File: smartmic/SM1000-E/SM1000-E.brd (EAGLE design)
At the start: 65 x 100 mm, 201 parts, among them CN1 HDR100-3, CN10 ST-3509, CN11 HDR100-3, CN12 HRS-A3C-16DA, CN13 CONN-BOOM-XH-2A, CN2 JS-MU3-002, CN3 DS-0518, CN4 RJ-45, CN5 ST-3509, CN6 ST-3509, CN7 ST-3509, CN8 ST-3509, CN9 ST-3509, J1 JMP-2PIN, J3 JMP-2PIN, J4 JMP-2PIN, P1 TPAD50, P10 TPAD50, P11 TPAD50, P12 TPAD50, P13 TPAD50, P14 TPAD50, P16 TPAD50, P18 TPAD50, P19 TPAD50, P2 TPAD50, P20 TPAD50, P3 TPAD50, P4 TPAD50, P5 TPAD50, P6 TPAD50, P7 TPAD50, P8 TPAD50, P9 TPAD50, SW1 SW-SPDT-8US8WR2C2M7RES, SW2 TS-026, SW3 DPDT, SW4 TS-026, SW5 TS-02B, SW6 SW-LC2259, SW7 SW-LC2259, T1 SM-LP-5001, T2 SM-LP-5001, U1 STM32F405VGT6, U2 LD3985M33R, U3 STMPS2141, U4 EMIF02-USB03F2, U5 TPS54329E, U6 LMV341, U7 LMV341, U8 LM386M-1, U9 LMV341

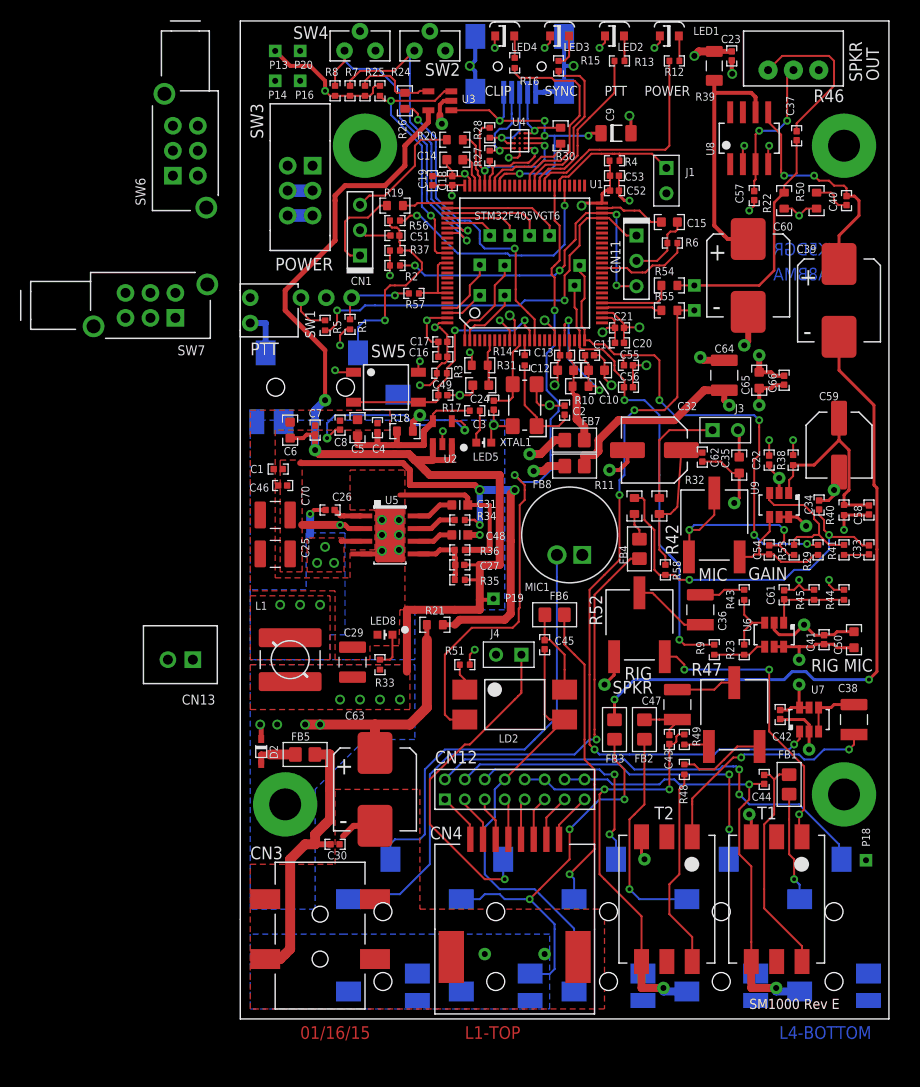
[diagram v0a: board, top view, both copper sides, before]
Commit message: IMPLEMENT CHANGES PER SM1000-E-CHANGE-LOG.TXT RGB
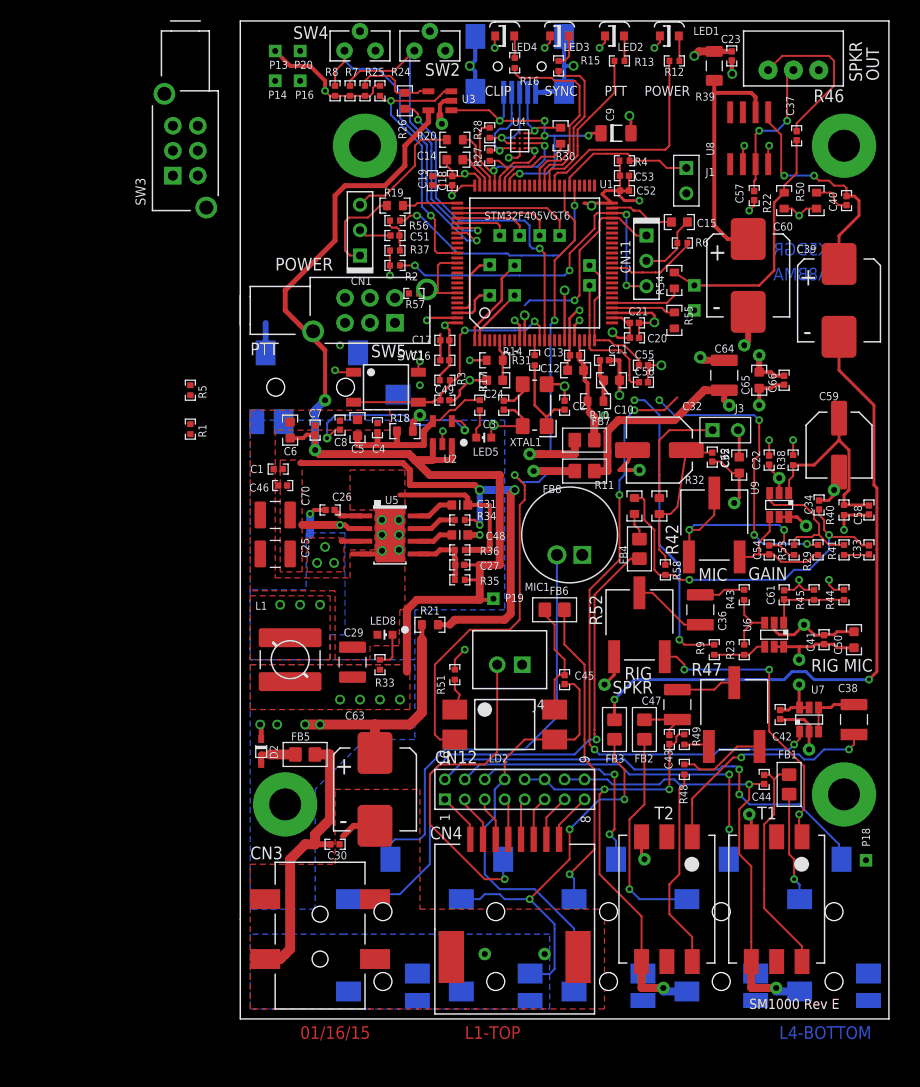
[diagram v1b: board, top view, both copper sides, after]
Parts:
- removed CN13: CONN-BOOM-XH-2A, _RoweTel:CONN-BOOM-XH-2A
- removed SW6, SW7: SW-LC2259, _RoweTel:SW-LC2259
- J4: value JMP-2PIN -> CONN-BOOM-XH-2A; device _Coherix:JMPR-2PIN -> _RoweTel:CONN-BOOM-XH-2A
- LED1: value LED-RED,RA -> LTST-S220KGKT
- LED2: value LED-RED,RA -> LTST-S220KRKT
- LED3: value LED-GRN,RA -> LTST-S220KGKT
- LED4: value LED-YEL,RA -> LTST-S220KRKT
- SW1: value SW-SPDT-8US8WR2C2M7RES -> SW-LC2259; device _RoweTel:SW-SPDT-8US8WR2C2M7RES -> _RoweTel:SW-LC2259
- SW3: value DPDT -> SW-LC2259EENP; device _RoweTel:SW-PWR -> _RoweTel:SW-LC2259
- moved R1 19.1 mm to (-5.00, 59.1)
- moved R5 15.0 mm to (-5.00, 63.0)
- moved SW3 12.2 mm to (-5.50, 87.0), turned to 270 degrees
- moved SW1 12.0 mm to (13.0, 71.0)
- moved C45 4.03 mm to (32.5, 34.0)
- moved LD2 2.24 mm to (26.5, 29.5)
- moved R10 2.12 mm to (35.6, 61.9)
- moved J1 2.00 mm to (44.7, 84.0)
- moved C10 1.80 mm to (37.2, 64.0)
- moved C11 1.58 mm to (36.5, 66.0)
- moved C20 1.58 mm to (39.5, 68.2)
- moved C21 1.58 mm to (39.5, 69.8)
- moved C56 1.58 mm to (40.4, 63.8)
- moved R31 1.58 mm to (25.5, 66.0)
- moved C55 1.50 mm to (40.4, 65.5)
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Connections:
- net +VIN: now also SW3.1, SW3.4; no longer SW3.3, SW3.6
- net GND: now also J4.1, SW1.7, SW1.8, SW3.7, SW3.8; no longer J4.2, SW1.G1, SW1.G2
- net N$14: now also SW1.1
- net N$62: now also J4.2; no longer J4.1
- net VDD: now also SW1.2, SW1.5; no longer SW1.6
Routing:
- net USART3_TX: track 40.9 -> 19.8 mm, vias 2 -> 1
- net N$15: track 20.2 -> 3.71 mm, vias 1 -> 0
- net DAC1_OUT: track 73.5 -> 63.1 mm
- net N$4: track 15.0 -> 6.42 mm
- net +VIN: track 170.7 -> 162.3 mm
- net N$14: track 8.15 -> 0.00 mm, vias 1 -> 0
- net AIN2: track 50.6 -> 43.3 mm
- net VDD: track 65.6 -> 71.0 mm
- net N$81: track 65.3 -> 60.0 mm
- net OSC_IN: track 8.03 -> 3.05 mm
- net N$74: track 8.77 -> 11.6 mm
- net OTG_PWR_ON: track 31.5 -> 33.7 mm
- net !BOOT0!: track 6.70 -> 8.70 mm
- net AIN1: track 46.7 -> 44.8 mm
- net GND: track 207.0 -> 208.8 mm, vias 52 -> 51
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
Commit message: 21  [X]         From Mel: DNL LED5 and LED8 to save a little power. 			DNL LED8	RGB 			DNL R33 			DNL LED5 			DNL R17
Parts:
- LED5: value SML-LX0603SRW-TR -> (none)
- LED8: value SML-LX0603SRW-TR -> DNL
- R17: value 1K,1% -> DNL
- R33: value 2.2K,1% -> DNL
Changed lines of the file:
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@@
 <attribute name="VALUE" x="7.0375" y="57.75" size="1" layer="27" font="vector" ratio="10" rot="R90"/>
 </element>
-<element name="R17" library="AA-ipc-7351-resistor" package="RESC1005X40AN" value="1K,1%" x="24" y="61.5" smashed="yes" rot="R90">
+<element name="R17" library="AA-ipc-7351-resistor" package="RESC1005X40AN" value="DNL" x="24" y="61.5" smashed="yes" rot="R90">
 <attribute name="NAME" x="23.9" y="64.8" size="0.8128" layer="25" font="vector" rot="R270"/>
 </element>
@@
 </element>
 <element name="SH3" library="_Coherix" package="NOPACKAGE" value="SHUNT,0.1IN" x="1.5" y="-0.5" locked="yes" smashed="yes" rot="R180"/>
-<element name="R33" library="AA-ipc-7351-resistor" package="RESC1005X40AN" value="2.2K,1%" x="14" y="35.5" smashed="yes" rot="R90">
+<element name="R33" library="AA-ipc-7351-resistor" package="RESC1005X40AN" value="DNL" x="14" y="35.5" smashed="yes" rot="R90">
 <attribute name="NAME" x="13.5" y="33.3" size="0.8128" layer="25" font="vector"/>
 </element>
@@
 <attribute name="NAME" x="34.5" y="92.8" size="1.27" layer="26" font="vector" ratio="10" rot="MR180"/>
 </element>
-<element name="LED8" library="_RoweTel" package="SML-LX0603SRW" value="SML-LX0603SRW-TR" x="14.5" y="38.5" smashed="yes">
+<element name="LED8" library="_RoweTel" package="SML-LX0603SRW" value="DNL" x="14.5" y="38.5" smashed="yes">
 <attribute name="NAME" x="13" y="39.5" size="0.8128" layer="25" ratio="10"/>
 </element>
-<element name="LED5" library="_RoweTel" package="SML-LX0603SRW" value="SML-LX0603SRW-TR" x="24.4" y="58.25" smashed="yes" rot="R180">
+<element name="LED5" library="_RoweTel" package="SML-LX0603SRW" value="" x="24.4" y="58.25" smashed="yes" rot="R180">
 <attribute name="NAME" x="25.9" y="57.25" size="0.8128" layer="25" ratio="10" rot="R180"/>
 </element>

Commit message: 4. [X] Add part outlines to layer tdoc for documentation.        Complete RGB
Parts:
- U3: device AA-IC:SOT23-5L -> _RoweTel:SOT23-5L
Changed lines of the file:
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@@
 <layer number="14" name="Route14" color="1" fill="6" visible="no" active="no"/>
 <layer number="15" name="VDD" color="6" fill="1" visible="no" active="yes"/>
-<layer number="16" name="Bottom" color="1" fill="1" visible="yes" active="yes"/>
-<layer number="17" name="Pads" color="2" fill="1" visible="yes" active="yes"/>
-<layer number="18" name="Vias" color="2" fill="1" visible="yes" active="yes"/>
+<layer number="16" name="Bottom" color="1" fill="1" visible="no" active="yes"/>
+<layer number="17" name="Pads" color="2" fill="1" visible="no" active="yes"/>
+<layer number="18" name="Vias" color="2" fill="1" visible="no" active="yes"/>
 <layer number="19" name="Unrouted" color="6" fill="1" visible="yes" active="yes"/>
 <layer number="20" name="Dimension" color="15" fill="1" visible="yes" active="yes"/>
@@
 <layer number="22" name="bPlace" color="7" fill="1" visible="no" active="yes"/>
 <layer number="23" name="tOrigins" color="15" fill="1" visible="yes" active="yes"/>
-<layer number="24" name="bOrigins" color="15" fill="1" visible="yes" active="yes"/>
+<layer number="24" name="bOrigins" color="15" fill="1" visible="no" active="yes"/>
 <layer number="25" name="tNames" color="7" fill="1" visible="no" active="yes"/>
 <layer number="26" name="bNames" color="7" fill="1" visible="no" active="yes"/>
@@
 <layer number="108" name="fp8" color="7" fill="1" visible="no" active="yes"/>
 <layer number="109" name="fp9" color="7" fill="1" visible="no" active="yes"/>
-<layer number="110" name="POTS" color="7" fill="1" visible="yes" active="yes"/>
+<layer number="110" name="POTS" color="7" fill="1" visible="no" active="yes"/>
 <layer number="116" name="Patch_BOT" color="7" fill="1" visible="no" active="yes"/>
 <layer number="121" name="tTestdril" color="7" fill="1" visible="no" active="yes"/>
@@
 <attribute name="NAME" x="31.6" y="86.05" size="0.8128" layer="25" font="vector"/>
 </element>
-<element name="U3" library="AA-IC" package="SOT23-5L" value="STMPS2141" x="20" y="92" locked="yes" smashed="yes" rot="R270">
+<element name="U3" library="_RoweTel" package="SOT23-5L" value="STMPS2141" x="20" y="92" smashed="yes" rot="R270">
 <attribute name="NAME" x="22.2" y="91.8" size="0.8128" layer="25" font="vector" ratio="10"/>
 </element>
@@
 <wire x1="60.5" y1="51.5" x2="62.95" y2="51.5" width="0.3" layer="1"/>
 <wire x1="62.95" y1="51.5" x2="63" y2="51.45" width="0.2" layer="1"/>
-<wire x1="60.5" y1="51.5" x2="60.5" y2="52.5" width="0.3" layer="1"/>
-<wire x1="60.5" y1="52.5" x2="61" y2="53" width="0.3" layer="1"/>
-<wire x1="61" y1="53" x2="61" y2="57" width="0.3" layer="1"/>
-<wire x1="61" y1="57" x2="60" y2="58" width="0.3" layer="1"/>
+<wire x1="60" y1="58" x2="61.5" y2="56.5" width="0.3" layer="1"/>
+<wire x1="61.5" y1="56.5" x2="61.5" y2="53.2" width="0.3" layer="1"/>
+<wire x1="61.5" y1="53.2" x2="60.6" y2="52.3" width="0.3" layer="1"/>
+<wire x1="60.6" y1="52.3" x2="60.5" y2="52.2" width="0.3" layer="1"/>
+<wire x1="60.5" y1="52.2" x2="60.5" y2="51.5" width="0.3" layer="1"/>
 </signal>
 <signal name="N$87">

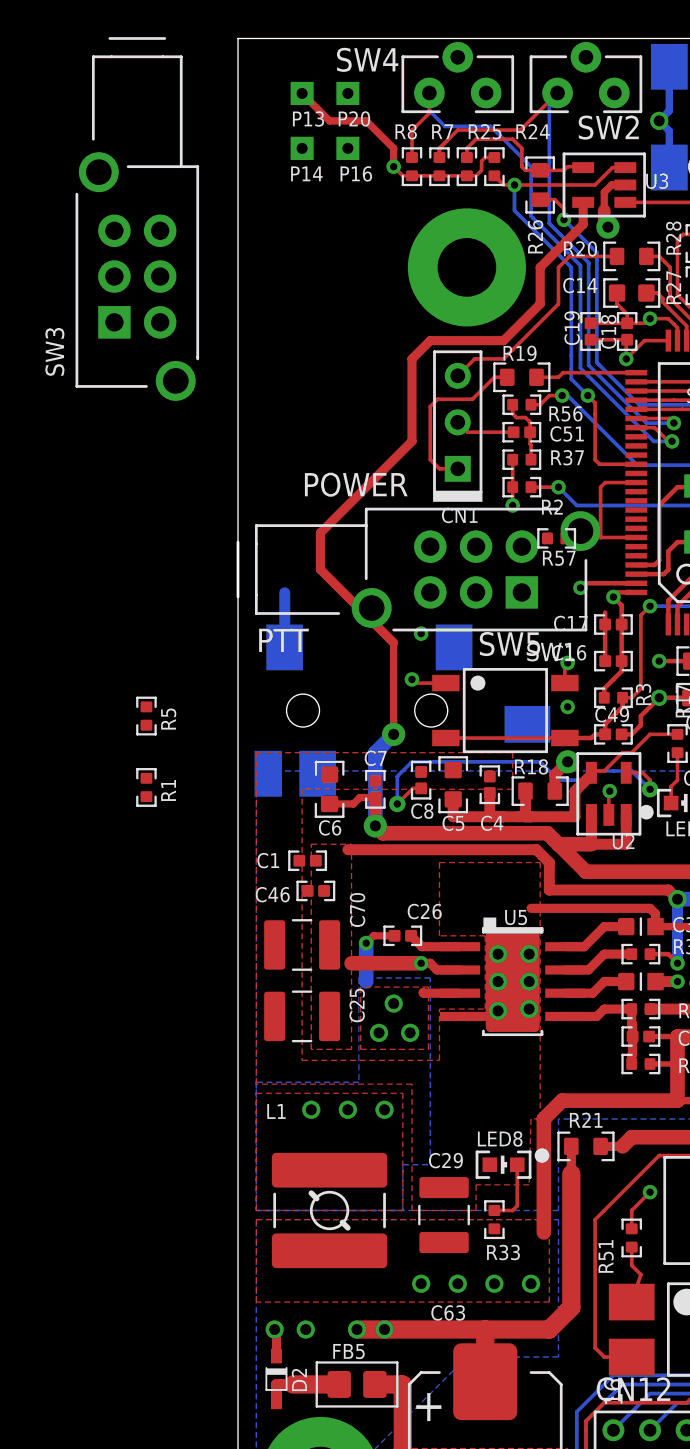
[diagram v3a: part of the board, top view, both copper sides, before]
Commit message: Added schematic power switch SW3 wiring change(.pngs) to accomodate PCB routing. Updated SM1000-E-change-log.txt file to reflect update and comments on #27 RGB
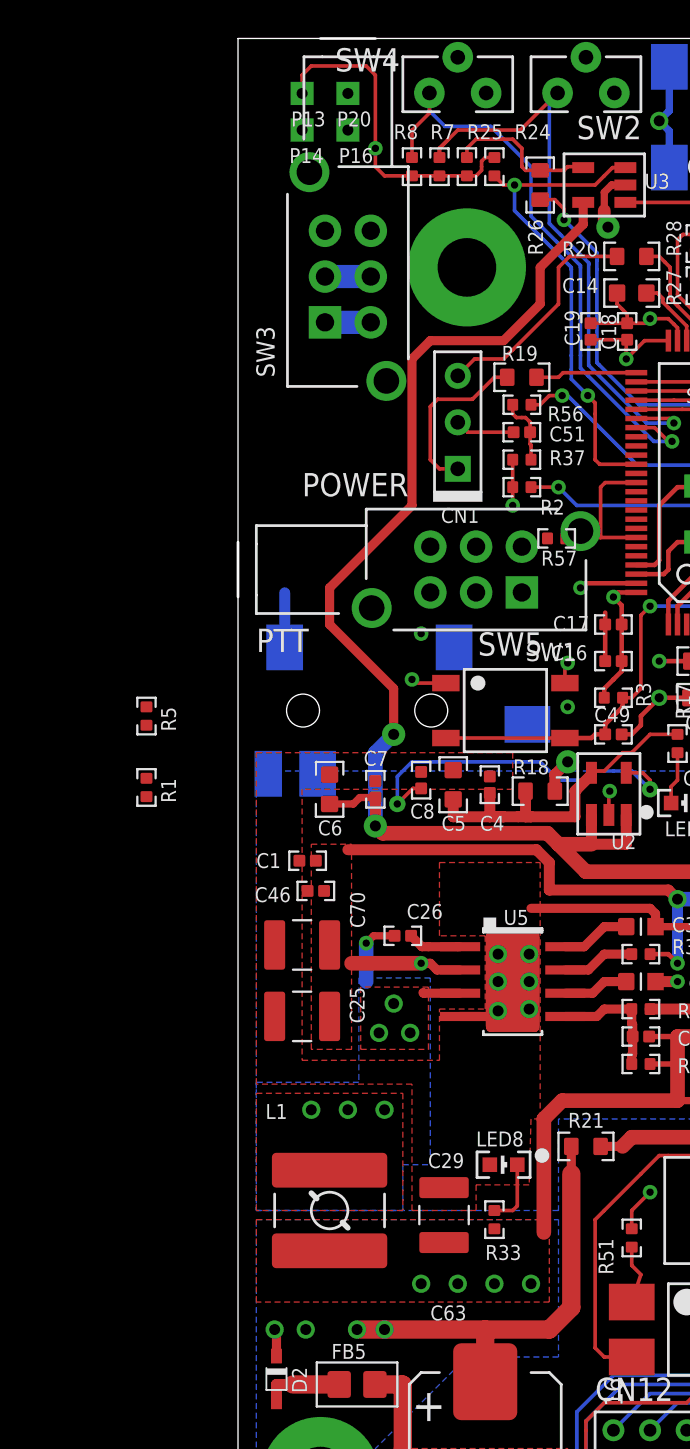
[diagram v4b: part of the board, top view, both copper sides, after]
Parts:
- moved SW3 11.5 mm to (6.00, 87.0)
- moved P14 1.00 mm to (3.50, 95.0)
- moved P16 1.00 mm to (6.00, 95.0)
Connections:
- net +VIN: now also SW3.2, SW3.5; no longer SW3.1, SW3.4
- net N$81: now also SW3.1, SW3.4; no longer SW3.2, SW3.5
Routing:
- net N$81: track 60.0 -> 66.8 mm
- net +VIN: track 162.3 -> 167.1 mm
- net VDD: track 71.0 -> 75.1 mm

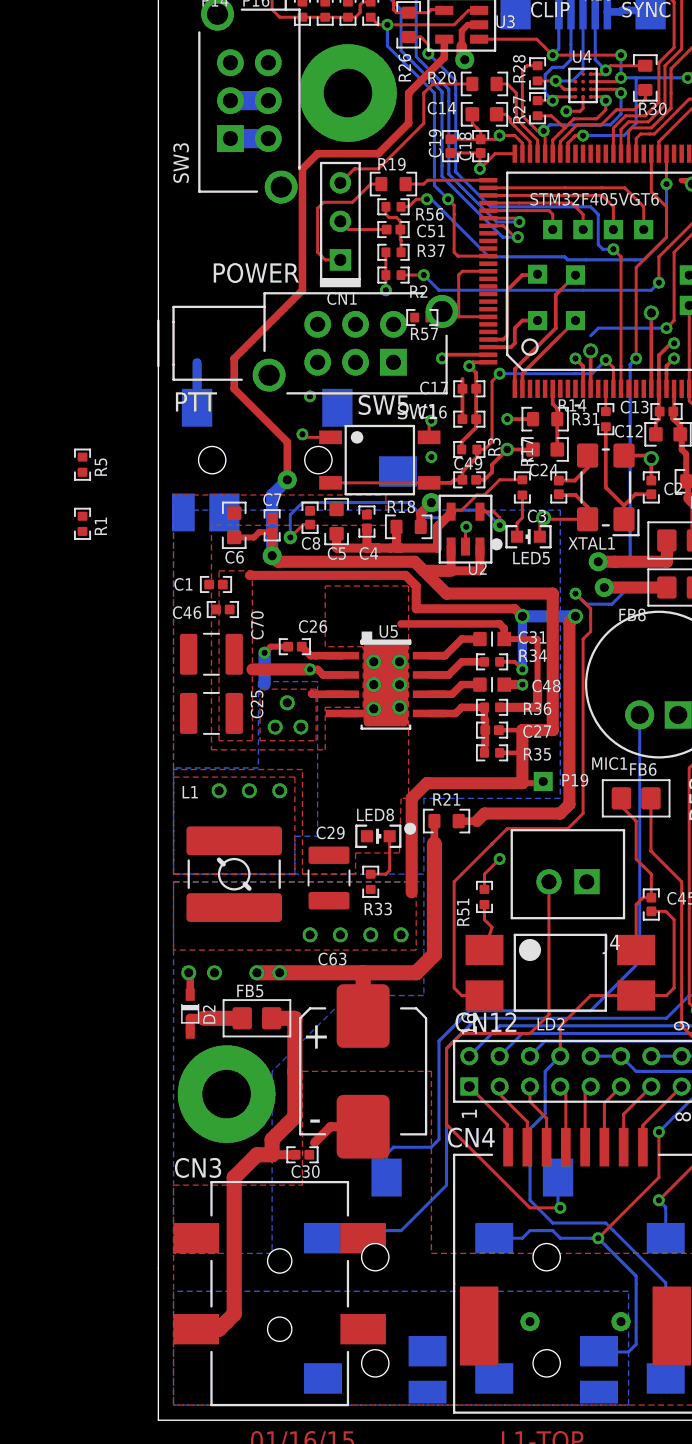
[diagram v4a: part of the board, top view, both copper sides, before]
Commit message: Added jmpr mono ext speaker situation. Update SM1000-E-change-log file. RGB
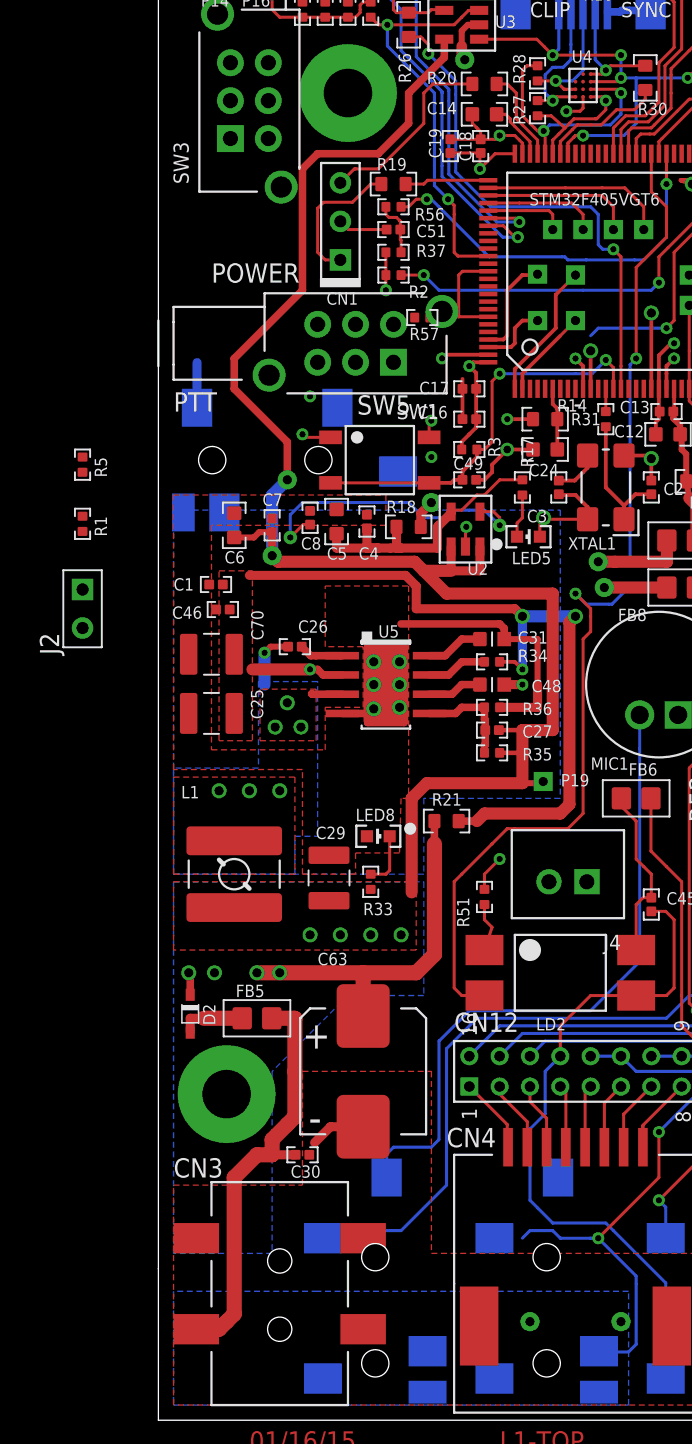
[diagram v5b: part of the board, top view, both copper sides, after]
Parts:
- added J2: JMP-2PIN, _Coherix:JMPR-2PIN
- added SH2: SHUNT,0.1IN, _Coherix:NOPACKAGE
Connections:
- new net N$83: CN8.B, J4.2
- net N$62: now also CN8.F, FB3.2, J2.2; no longer CN8.D, J4.2
- net N$75: now also J2.1; no longer CN8.B, FB3.2
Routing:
- net N$75: track 39.8 -> 0.00 mm, vias 3 -> 0
- net +VIN: track 167.1 -> 159.1 mm
- net N$81: track 66.8 -> 61.5 mm
- net N$62: track 33.3 -> 37.9 mm, vias 1 -> 3
